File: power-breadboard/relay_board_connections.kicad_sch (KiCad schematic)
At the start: 17 parts, among them J5 RA25S

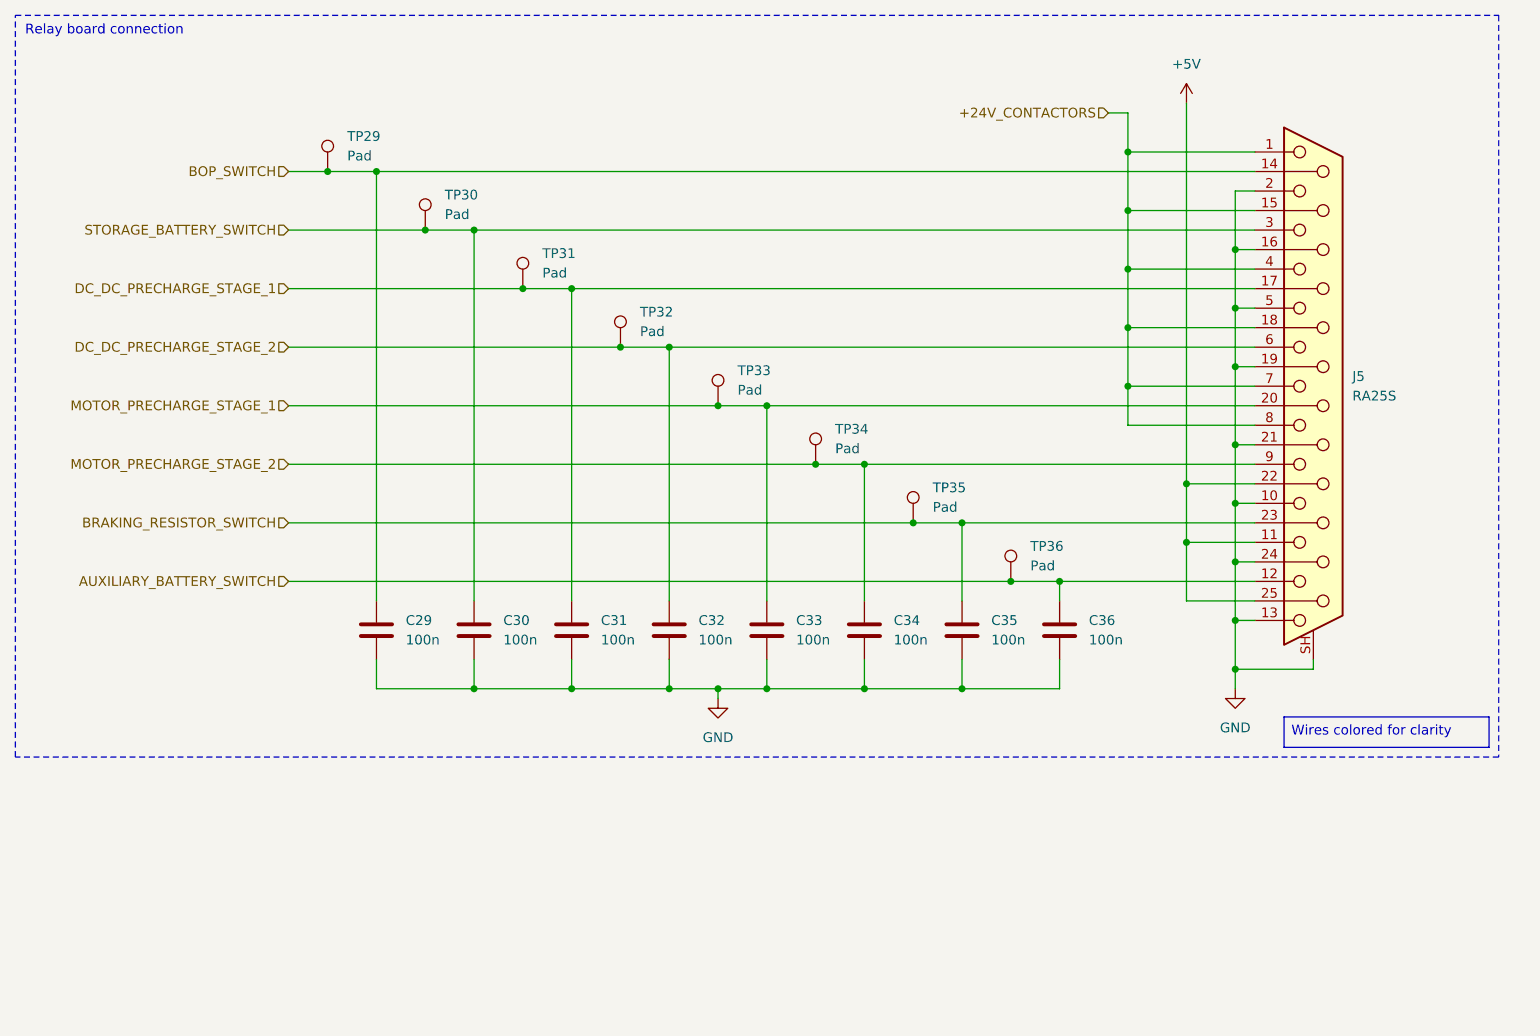
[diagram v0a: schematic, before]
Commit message: power-breadboard: finish relay board connections
Updateed to use separarate relay boards. Also updated hierarchical
labels and sheet pins.
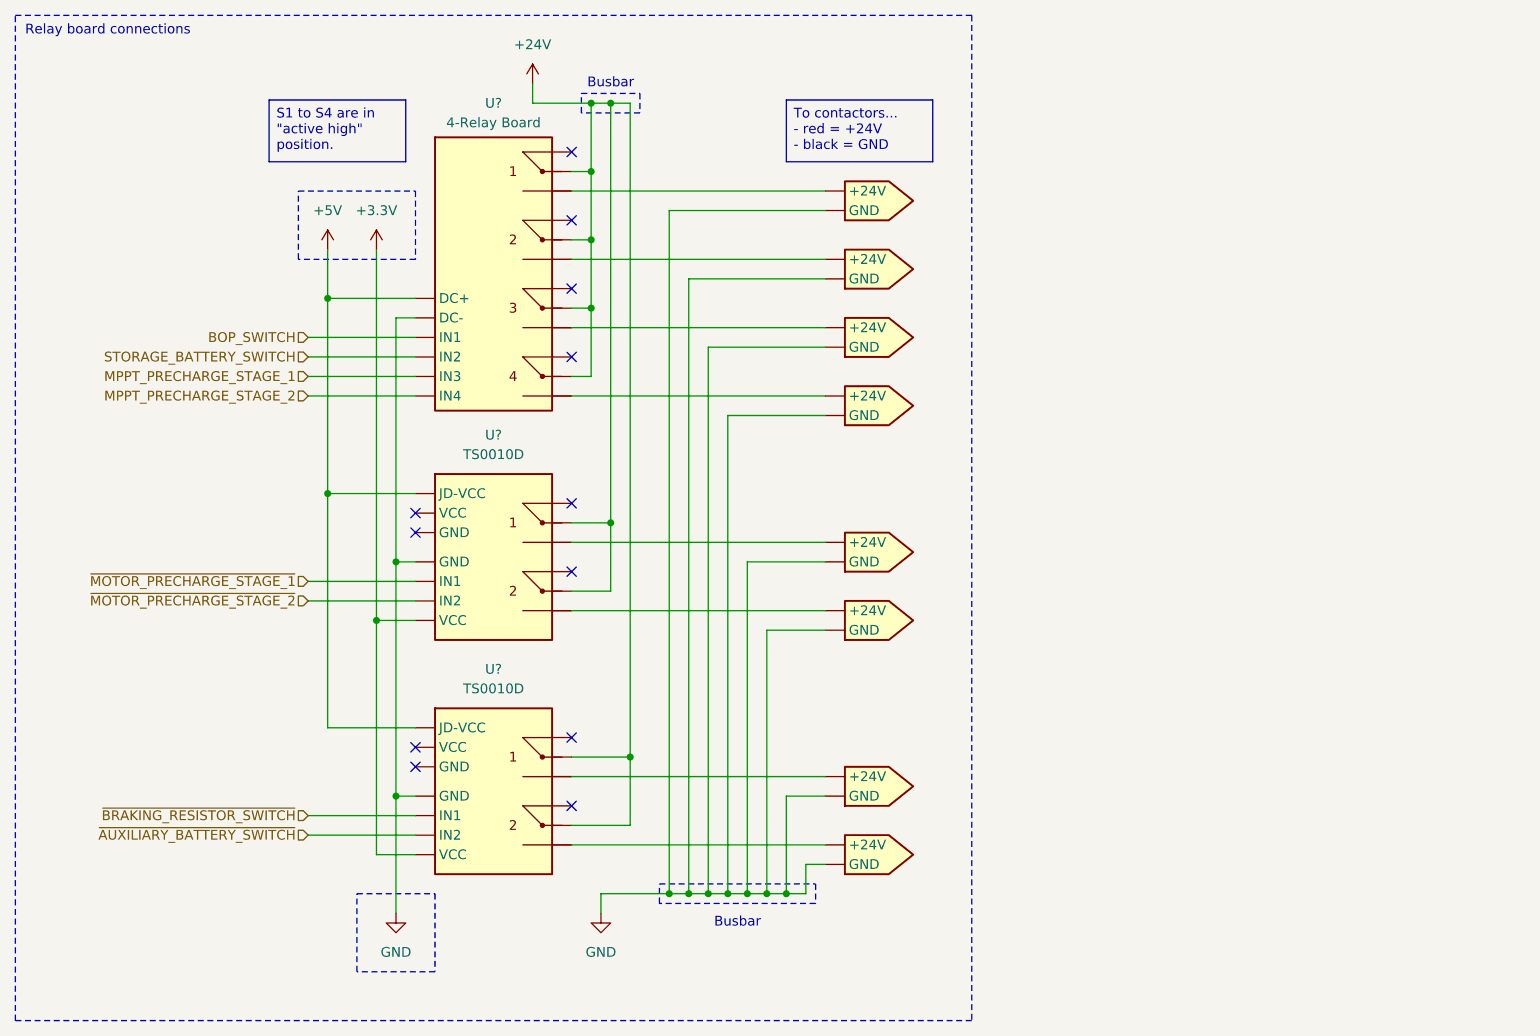
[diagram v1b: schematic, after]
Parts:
- removed C29, C30, C31, C32, C33, C34, C35, C36: 100n, Capacitor_SMD:C_0402_1005Metric_Pad0.74x0.62mm_HandSolder, symbol Device:C
- removed J5: RA25S, Connector_Dsub:DSUB-25_Socket_Horizontal_P2.77x2.84mm_EdgePinOffset7.70mm_Housed_MountingHolesOffset9.12mm, symbol Connector:DB25_Socket_MountingHoles
- removed TP29, TP30, TP31, TP32, TP33, TP34, TP35, TP36: Pad, TestPoint:TestPoint_Pad_D1.5mm, symbol Connector:TestPoint
- added #OUT1, #OUT2, #OUT3, #OUT4, #OUT5, #OUT6, #OUT7, #OUT8: (no value), symbol Exocet:Contactor_Output
- added U?: (no value), symbol Exocet:Relay_Board_4
- added U? (x2): TS0010D, symbol Exocet:TS0010D
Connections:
- net +5V: now also U?., U?., U?.
- net BOP_SWITCH: now also U?.
- net GND: now also #OUT1. (GND), #OUT2. (GND), #OUT3. (GND), #OUT4. (GND), #OUT5. (GND), #OUT6. (GND), #OUT7. (GND), #OUT8. (GND), U?., U?., U?.
- net STORAGE_BATTERY_SWITCH: now also U?.
- new net: #OUT3. (GND), U?.
- new net: #OUT2. (GND), U?.
- new net: #OUT4. (GND), U?.
- new net: #OUT1. (GND), U?.
- new net: #OUT6. (GND), U?.
- new net: #OUT7. (GND), U?.
- new net: #OUT8. (GND), U?.
- new net: #OUT5. (GND), U?.
- new net +24V: U?., U?., U?.
- new net +3.3V: U?., U?.
- new net MPPT_PRECHARGE_STAGE_1: U?.
- new net MPPT_PRECHARGE_STAGE_2: U?.
- new net ~{AUXILIARY_BATTERY_SWITCH}: U?.
- new net ~{BRAKING_RESISTOR_SWITCH}: U?.
- new net ~{MOTOR_PRECHARGE_STAGE_1}: U?.
- new net ~{MOTOR_PRECHARGE_STAGE_2}: U?.
- no-connect marks 0 -> 12
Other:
- note added: "Busbar"
- note added: "Relay board connections"
- note removed: "Relay board connection"

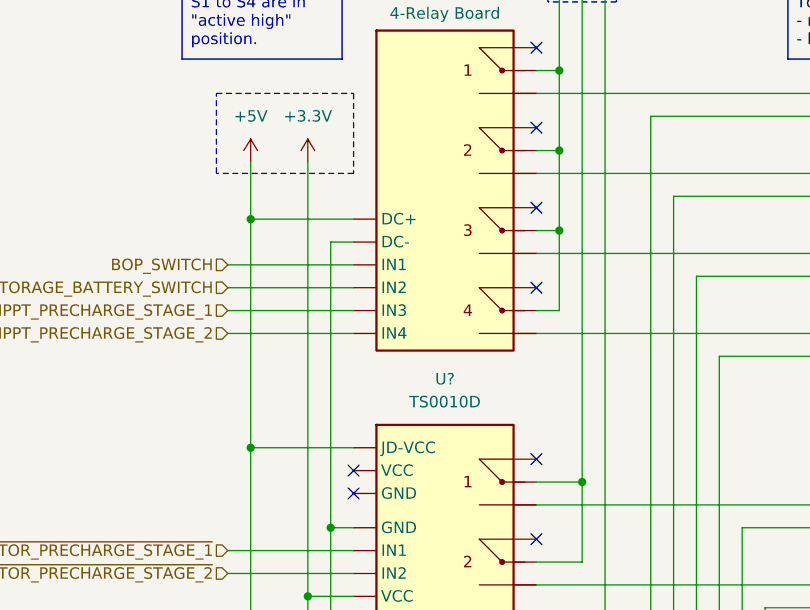
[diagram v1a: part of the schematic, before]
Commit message: power-breadboard: change DC+ of 4-relay board
Needs to be 24V instead of 5V.
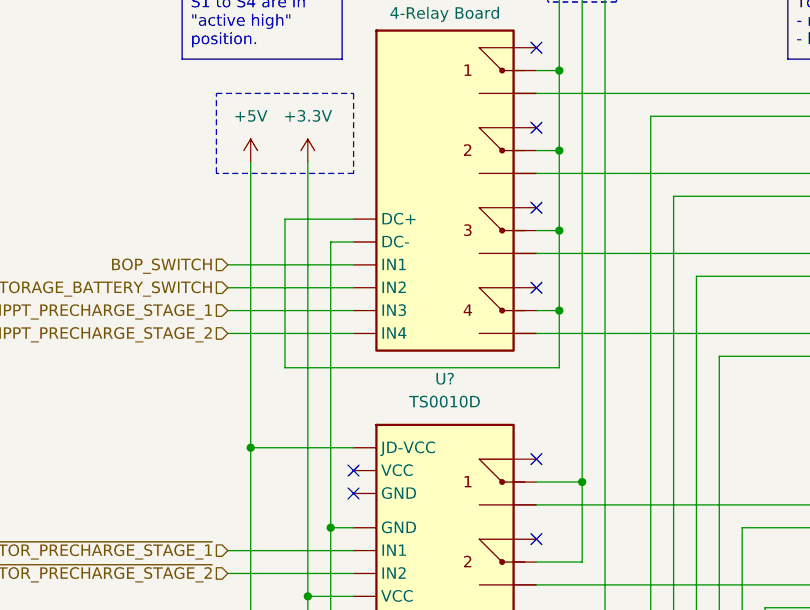
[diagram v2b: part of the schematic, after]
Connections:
- net +5V: no longer U?.
- new net: #OUT3. (GND), U?.
- new net: #OUT2. (GND), U?.
- new net: #OUT4. (GND), U?.
- new net: #OUT1. (GND), U?.
- new net: #OUT6. (GND), U?.
- new net: #OUT7. (GND), U?.
- new net: #OUT8. (GND), U?.
- new net: #OUT5. (GND), U?.
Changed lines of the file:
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@@
+	)
+	(junction
+		(at 87.63 59.69)
+		(diameter 0)
+		(color 221 133 0 1)
 	)
 	(junction
@@
 	)
 	(junction
-		(at 53.34 49.53)
-		(diameter 0)
-		(color 0 0 0 0)
-	)
-	(junction
 		(at 87.63 50.8)
 		(diameter 0)
@@
 	(wire
 		(pts
+			(xy 87.63 59.69) (xy 87.63 66.04)
+		)
+		(stroke
+			(width 0)
+			(type default)
+			(color 221 133 0 1)
+		)
+	)
+	(wire
+		(pts
 			(xy 85.09 118.11) (xy 92.71 118.11)
 		)
@@
 	(wire
 		(pts
-			(xy 53.34 49.53) (xy 53.34 43.18)
-		)
-		(stroke
-			(width 0)
-			(type default)
-		)
-	)
-	(wire
-		(pts
 			(xy 100.33 46.99) (xy 100.33 127)
 		)
@@
 	(wire
 		(pts
+			(xy 57.15 49.53) (xy 64.77 49.53)
+		)
+		(stroke
+			(width 0)
+			(type default)
+			(color 221 133 0 1)
+		)
+	)
+	(wire
+		(pts
 			(xy 110.49 92.71) (xy 110.49 127)
 		)
@@
 	(wire
 		(pts
+			(xy 87.63 66.04) (xy 57.15 66.04)
+		)
+		(stroke
+			(width 0)
+			(type default)
+			(color 221 133 0 1)
+		)
+	)
+	(wire
+		(pts
 			(xy 85.09 59.69) (xy 87.63 59.69)
 		)
@@
 	(wire
 		(pts
+			(xy 57.15 66.04) (xy 57.15 49.53)
+		)
+		(stroke
+			(width 0)
+			(type default)
+			(color 221 133 0 1)
+		)
+	)
+	(wire
+		(pts
 			(xy 118.11 83.82) (xy 107.95 83.82)
 		)
@@
 	(wire
 		(pts
-			(xy 53.34 74.93) (xy 53.34 49.53)
+			(xy 53.34 43.18) (xy 53.34 74.93)
 		)
 		(stroke
@@
 		)
 	)
-	(wire
-		(pts
-			(xy 53.34 49.53) (xy 64.77 49.53)
-		)
-		(stroke
-			(width 0)
-			(type default)
-		)
-	)
